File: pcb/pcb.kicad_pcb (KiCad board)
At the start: 2 copper layers, 3 parts

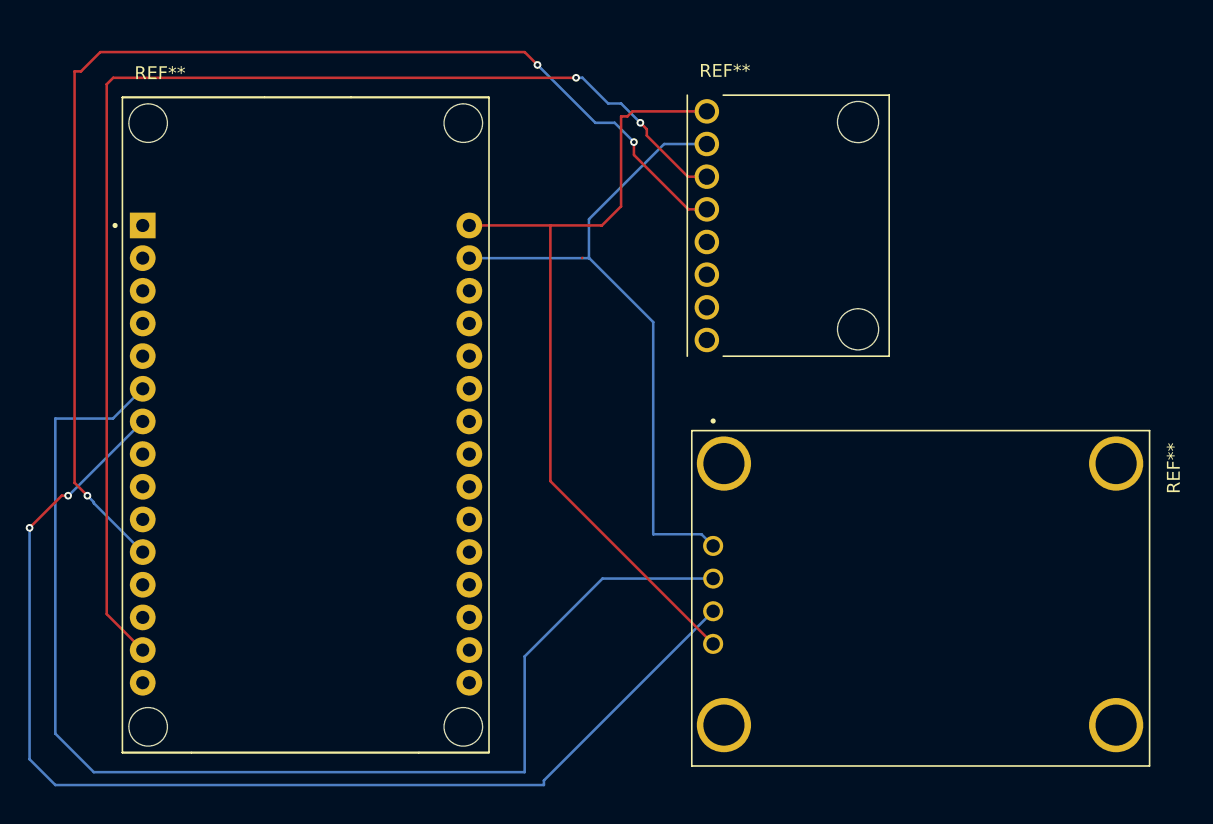
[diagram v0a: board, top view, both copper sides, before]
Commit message: suporte a DWM1000 e PCB
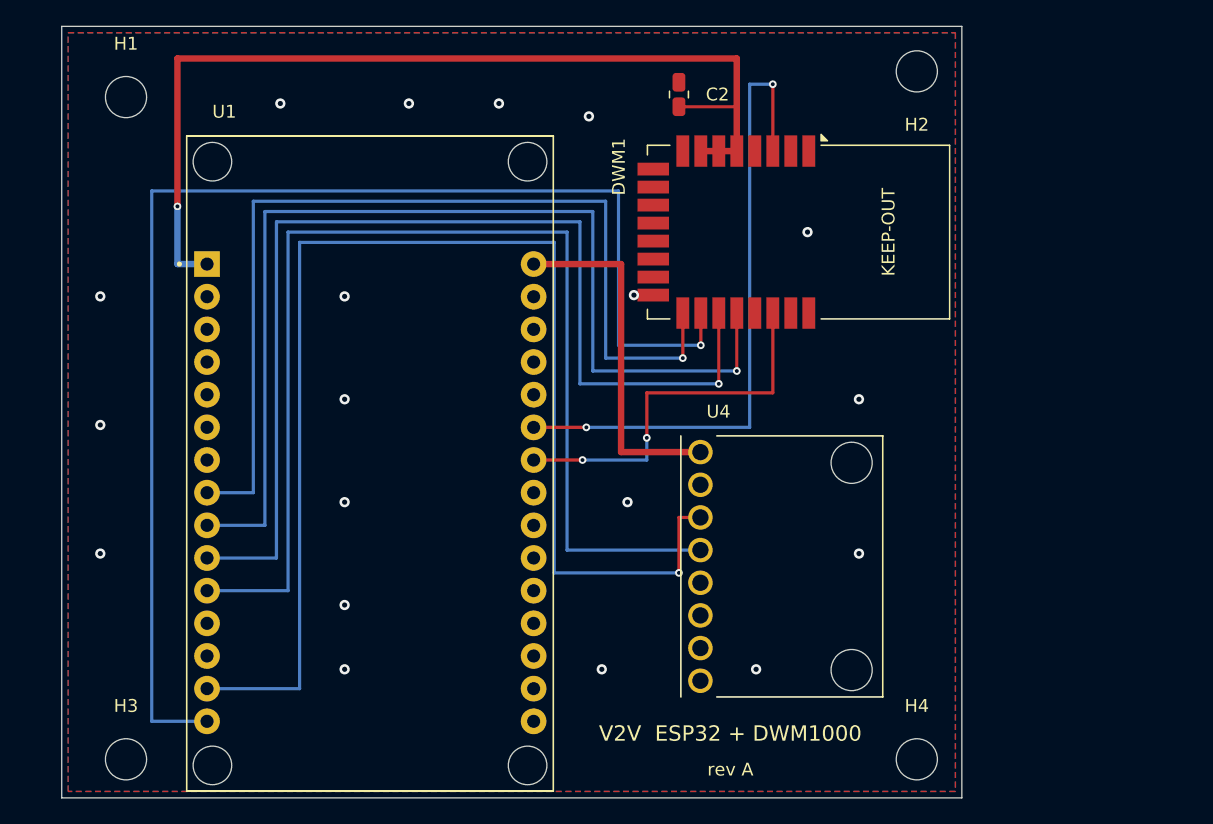
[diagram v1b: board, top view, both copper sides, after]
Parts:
- removed REF**: XCVR_ZC323200, gy-neo6mv2:XCVR_ZC323200
- added C2: 100nF, Capacitor_SMD:C_0805_2012Metric, F.Cu at (126.0, 34.3)
- added DWM1: DWM1000, RF_Module:DWM1000, F.Cu at (135.3, 45.0)
- added H1: MountingHole_3.2mm_M3, MountingHole:MountingHole_3.2mm_M3, F.Cu at (83.0, 34.5)
- added H2: MountingHole_3.2mm_M3, MountingHole:MountingHole_3.2mm_M3, F.Cu at (144.5, 32.5)
- added H3: MountingHole_3.2mm_M3, MountingHole:MountingHole_3.2mm_M3, F.Cu at (83.0, 86.0)
- added H4: MountingHole_3.2mm_M3, MountingHole:MountingHole_3.2mm_M3, F.Cu at (144.5, 86.0)
- U1: renamed from REF**; value MODULE_ESP32_DEVKIT_V1 -> ESP32-DEVKIT-V1
- U4: renamed from REF**; value MODULE_GY-521 -> GY-521
- moved U4 26.5 mm to (134.0, 71.0)
- moved U1 5.83 mm to (102.0, 63.0)
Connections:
- U1 pad 1: (no net) -> +3V3
- U1 pad 10: (no net) -> /UWB_MISO
- U1 pad 11: (no net) -> /I2C_SDA
- U1 pad 12: (no net) -> unconnected-(U1-RX0-Pad12)
- U1 pad 13: (no net) -> unconnected-(U1-TX0-Pad13)
- U1 pad 14: (no net) -> /I2C_SCL
- U1 pad 15: (no net) -> /UWB_MOSI
- U1 pad 16: (no net) -> unconnected-(U1-EN-Pad16)
- U1 pad 17: (no net) -> unconnected-(U1-VP-Pad17)
- U1 pad 18: (no net) -> unconnected-(U1-VN-Pad18)
- U1 pad 19: (no net) -> unconnected-(U1-D34-Pad19)
- U1 pad 2: (no net) -> GND
- U1 pad 20: (no net) -> unconnected-(U1-D35-Pad20)
- U1 pad 21: (no net) -> unconnected-(U1-D32-Pad21)
- U1 pad 22: (no net) -> unconnected-(U1-D33-Pad22)
- U1 pad 23: (no net) -> unconnected-(U1-D25-Pad23)
- U1 pad 24: (no net) -> /UWB_IRQ
- U1 pad 25: (no net) -> /UWB_RST
- U1 pad 26: (no net) -> unconnected-(U1-D14-Pad26)
- U1 pad 27: (no net) -> unconnected-(U1-D12-Pad27)
- U1 pad 28: (no net) -> unconnected-(U1-D13-Pad28)
- U1 pad 29: (no net) -> GND
- U1 pad 3: (no net) -> unconnected-(U1-D15-Pad3)
- U1 pad 30: (no net) -> +5V
- U1 pad 4: (no net) -> unconnected-(U1-D2-Pad4)
- U1 pad 5: (no net) -> unconnected-(U1-D4-Pad5)
- U1 pad 6: (no net) -> unconnected-(U1-RX2-Pad6)
- U1 pad 7: (no net) -> unconnected-(U1-TX2-Pad7)
- U1 pad 8: (no net) -> /UWB_CS
- U1 pad 9: (no net) -> /UWB_SCK
- U4 pad AD0: (no net) -> unconnected-(U4-PadAD0)
- U4 pad GND: (no net) -> GND
- U4 pad INT: (no net) -> unconnected-(U4-PadINT)
- U4 pad SCL: (no net) -> /I2C_SCL
- U4 pad SDA: (no net) -> /I2C_SDA
- U4 pad VCC: (no net) -> +5V
- U4 pad XCL: (no net) -> unconnected-(U4-PadXCL)
- U4 pad XDA: (no net) -> unconnected-(U4-PadXDA)
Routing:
- net (no net): track 493.3 -> 0.00 mm, vias 7 -> 0
- net /I2C_SCL: track 0.00 -> 103.1 mm, vias 0 -> 1
- net /UWB_MOSI: track 0.00 -> 102.7 mm, vias 0 -> 1
- net /I2C_SDA: track 0.00 -> 91.0 mm
- net /UWB_MISO: track 0.00 -> 84.0 mm, vias 0 -> 1
- net /UWB_SCK: track 0.00 -> 82.5 mm, vias 0 -> 1
- net +3V3: track 0.00 -> 76.3 mm, vias 0 -> 1
- net /UWB_CS: track 0.00 -> 75.4 mm, vias 0 -> 1
- net /UWB_RST: track 0.00 -> 50.5 mm, vias 0 -> 2
- net /UWB_IRQ: track 0.00 -> 30.0 mm, vias 0 -> 2
- net +5V: track 0.00 -> 27.6 mm
- net GND: track 0.00 -> 1.50 mm, vias 0 -> 19
- added copper zone on B.Cu, net GND
- added copper zone on F.Cu, net GND
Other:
- board outline added: 70 x 60 mm
- board text added: "KEEP-OUT"
- board text added: "V2V ESP32 + DWM1000"
- board text added: "rev A"
